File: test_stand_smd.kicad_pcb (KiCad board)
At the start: 2 copper layers, 15.7 x 28.7 mm, 23 parts, among them J1 Conn_01x05_Male, J2 USB_C_Receptacle_USB2.0, U1 ATSAMD21E, U2 AP2112K-3.3

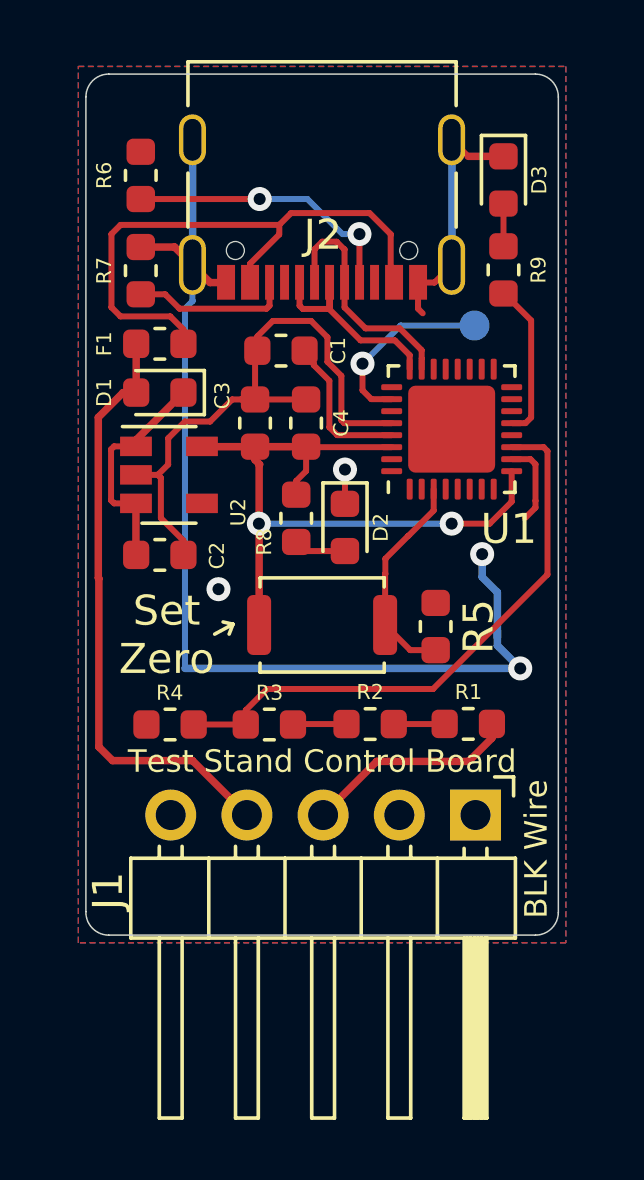
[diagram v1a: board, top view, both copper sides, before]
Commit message: upgraded to kicad 6
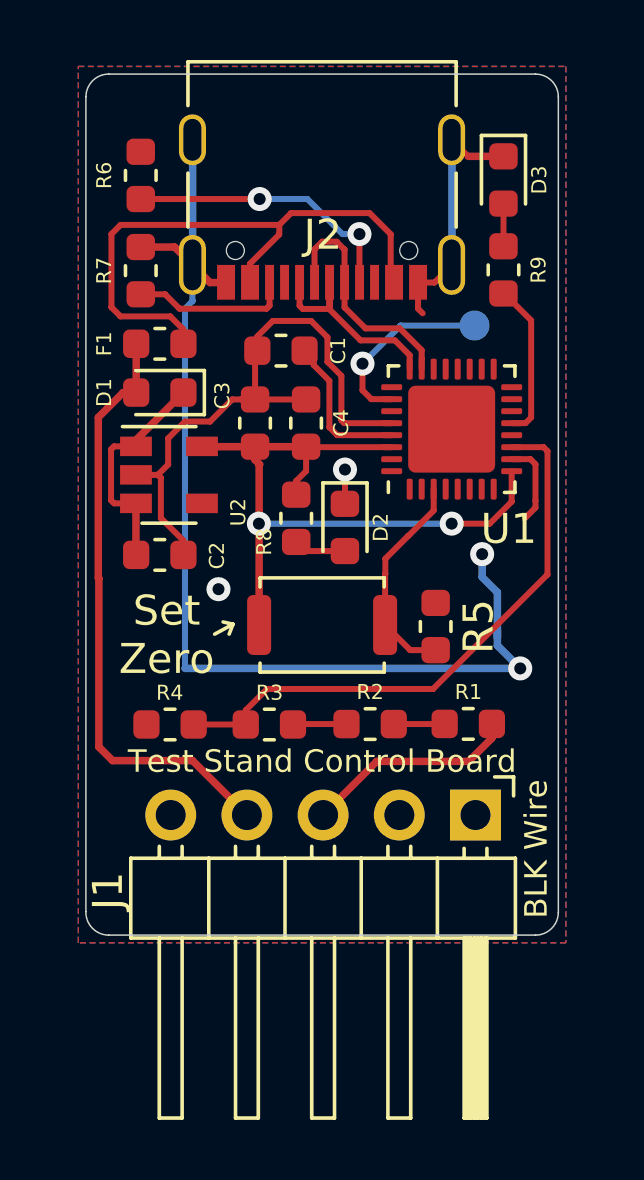
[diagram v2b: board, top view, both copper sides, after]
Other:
- net class Default removed
